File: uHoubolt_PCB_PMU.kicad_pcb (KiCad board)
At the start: 4 copper layers, 118 x 118 mm, 176 parts, among them J10 Debug, J11 AltimaxPwr, J12 CAN1, J13 CAN2, J14 CAN1, J15 CAN2, J16 CAN1, J17 CAN2, J18 CAN1, J19 CAN2, J2 Battery, J20 Output, J21 Output, J22 Output, J23 Payload, J24 Output, J25 RCU, J27 Umbilical0, J28 Umbilical0, J29 AltimaxArm, J3 Power, J4 BatteryAltimax, J5 Umbilical1, J6 AltimaxArm, J8 Altimax_PWR, J9 Debug, Q1 BSZ0905PNSATMA1, Q2 BSZ0902NSATMA1, Q3 SISA88DN or similar, Q4 SISA88DN or similar, Q5 SISA88DN or similar, Q6 SISA88DN or similar, Q7 SISA88DN or similar, SW1 Power_1, SW2 Power_2, SW3 Pyro_1, SW4 Pyro_2, U1 LM5069, U10 ICM-20602, U11 LPS25HB, U12 SFH617A-1X007T, U13 TS30041, U14 LiIon_Charger, U15 SFH617A-1X007T, U2 LMP8640 F, U3 TS30041, U4 LiIon_Charger, U5 STM32G491MET6-LQFP80, U6 W25Q256JV, U7 MCP1700-3302E, U8 MCP2562FDx-x_MF, U9 MCP2562FDx-x_MF, X1 TXC-7C

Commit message: V3 Updated ready for check
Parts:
- removed J11: AltimaxPwr, TXV_Library_Footprints:Molex_SL_1x2_Vertical
- removed J29: AltimaxArm, TXV_Library_Footprints:Molex_Nano-Fit_105309-xx02_1x02_P2.50mm_Vertical
- removed J6: AltimaxArm, TXV_Library_Footprints:Molex_SL_1x2_Vertical
- removed J8: Altimax_PWR, TXV_Library_Footprints:Molex_SL_1x2_Vertical
- added J1: Conn_01x04, TXV_Library_Footprints:Molex_Nano-Fit_105309-xx04_1x04_P2.50mm_Vertical, F.Cu at (181.4, 117.1)
- added J7: Conn_01x04, TXV_Library_Footprints:Molex_Nano-Fit_105309-xx04_1x04_P2.50mm_Vertical, F.Cu at (165.5, 69.8)
- J27: moved to B.Cu
- moved J25 33.0 mm to (141.2, 45.7)
- moved R23 27.8 mm to (97.9, 117.5), turned to -90 degrees
- moved D3 24.8 mm to (97.9, 120.5), turned to 90 degrees
- moved J23 20.2 mm to (145.7, 132.1), turned to 180 degrees
- moved J24 15.6 mm to (145.2, 147.0), turned to 90 degrees
- moved J28 14.0 mm to (169.8, 59.6), turned to 90 degrees
- moved D18 13.8 mm to (146.4, 143.4), turned to 0 degrees
- moved JP7 12.5 mm to (141.4, 146.8), turned to 90 degrees
- moved Q7 11.8 mm to (146.2, 140.2), turned to 0 degrees
- moved J27 11.3 mm to (159.7, 52.8), turned to 0 degrees
- moved R25 9.28 mm to (113.2, 127.7), turned to 180 degrees
- moved U12 8.67 mm to (137.2, 130.8), turned to 0 degrees
- moved R24 8.38 mm to (116.2, 127.7), turned to 180 degrees
- moved J20 8.29 mm to (114.0, 144.8)
- moved Q4 8.29 mm to (114.9, 138.1)
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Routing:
- net PYRO: track 171.7 -> 204.4 mm, vias 0 -> 2
- net /Out0: track 41.8 -> 51.4 mm
- net /Pyro_Sense: track 42.7 -> 35.2 mm
- net /Out3: track 61.8 -> 69.0 mm
- net /Out2: track 65.0 -> 58.5 mm
- net +5VP: track 92.8 -> 86.4 mm
- net +5V: track 146.7 -> 152.5 mm, vias 11 -> 9
- net Net-(J1-Pad3): track 7.75 -> 13.5 mm
- net /Vcharge: track 51.9 -> 57.4 mm, vias 1 -> 6
- net +12V: track 14.2 -> 9.72 mm, vias 10 -> 11
- net /CAN1_TX: track 41.3 -> 38.3 mm
- net Net-(J1-Pad4): track 9.04 -> 6.23 mm
- net /Speaker: track 9.73 -> 12.5 mm
- net /CAN1_RX: track 43.2 -> 40.7 mm
- net +3V3: track 116.6 -> 118.4 mm
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- added copper zone on B.Cu, net /Vcharge

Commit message: V3 2. Update ready for check
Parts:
- moved D25 7.47 mm to (129.8, 128.5)
- moved R56 4.24 mm to (129.1, 130.8), turned to 90 degrees
- moved R36 3.30 mm to (119.7, 138.9), turned to -90 degrees
- moved J2 2.89 mm to (115.3, 68.5), turned to 0 degrees
- moved D17 2.00 mm to (142.6, 136.5)
- moved D18 2.00 mm to (146.4, 141.5)
- moved J24 2.00 mm to (145.2, 145.0)
- moved JP7 2.00 mm to (141.4, 144.9)
- moved Q7 2.00 mm to (146.2, 138.3)
- moved R42 2.00 mm to (142.7, 138.1)
- moved R48 2.00 mm to (140.2, 138.9)
- moved R49 2.00 mm to (142.7, 139.7)
- moved D14 1.83 mm to (132.4, 136.5)
- moved D15 1.83 mm to (136.2, 141.5)
- moved J22 1.83 mm to (134.9, 145.0)
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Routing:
- net Net-(J4-Pad1): track 37.3 -> 0.00 mm
- net /Vcharge1: track 48.0 -> 37.3 mm
- net PYRO: track 204.4 -> 198.8 mm
- net /Out1: track 54.2 -> 51.8 mm
- net /Out3: track 69.0 -> 67.1 mm
- net /Out2: track 58.5 -> 56.6 mm
- net /Payload: track 64.6 -> 62.9 mm
- net +5VP: track 86.4 -> 85.4 mm
- net GND: vias 177 -> 186
- added copper zone on F.Cu, net /Vcharge1
- added copper zone on F.Cu, net Net-(J4-Pad1)

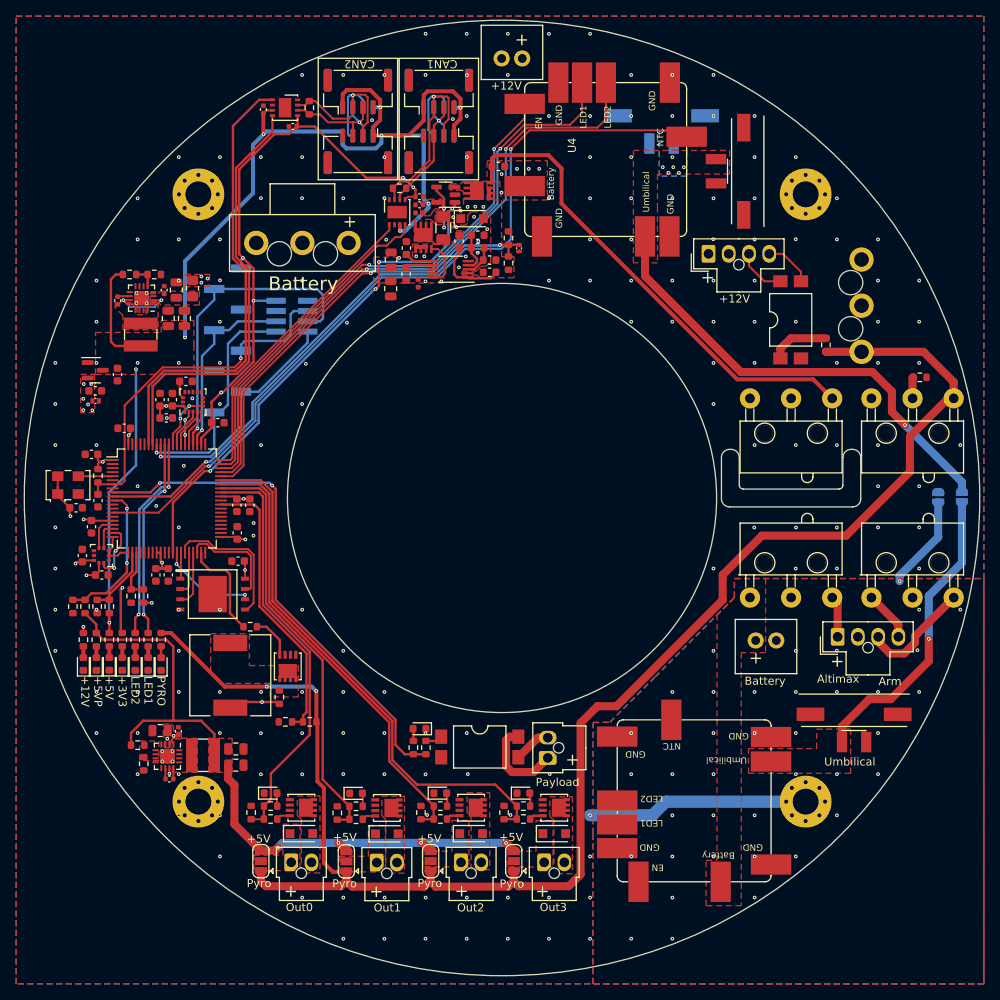
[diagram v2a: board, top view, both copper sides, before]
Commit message: Update of v3
Changed the silkscreen + more pads
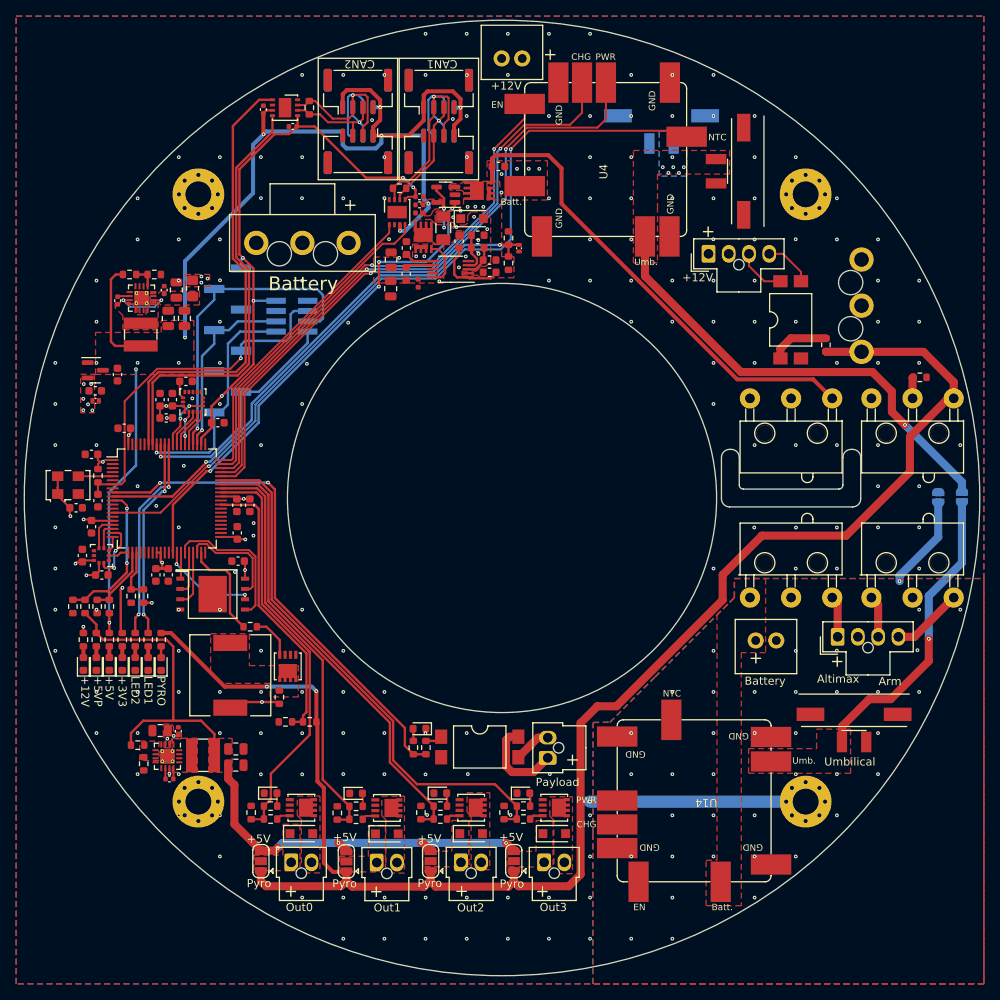
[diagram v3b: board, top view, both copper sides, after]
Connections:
- SW4 pad 1: Net-(J1-Pad4) -> Net-(J1-Pad3)
- SW4 pad 2: Net-(J1-Pad3) -> Net-(J1-Pad4)
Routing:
- net Net-(J1-Pad3): track 13.9 -> 5.19 mm
- net Net-(J1-Pad4): track 6.23 -> 8.84 mm
- net /Payload: track 62.9 -> 62.2 mm
- net GND: track 27.3 -> 26.7 mm, vias 186 -> 189
- net +12V: vias 11 -> 10
